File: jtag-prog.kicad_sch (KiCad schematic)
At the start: 38 parts, among them J5 USB_C_Receptacle_USB2.0_14P, J6 Conn_ST_STDC14, U14 AMS1117-3.3, U16 FT2232HQ, U17 93LCxxA, Y2 12Mhz

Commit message: Update the design files
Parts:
- C24: value 10uF -> 1uF
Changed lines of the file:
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@@
 			)
 		)
-		(property "Value" "10uF"
+		(property "Value" "1uF"
 			(at 113.03 67.3162 0)
 			(effects

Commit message: Update the schematic
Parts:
- added D9: D_Schottky, Diode_SMD:D_SOD-123, symbol Device:D_Schottky
- renumbered C18 to C36, C26 to C37, C21 to C38, C22 to C39, C16 to C40, C17 to C41, C48 to C42, C25 to C43, C49 to C44, C24 to C45, C23 to C46, C50 to C47, C54 to C48, C53 to C49, C52 to C50, J5 to J14, J6 to J15, R59 to R56, R35 to R57, R48 to R58, R60 to R59, R62 to R60, R63 to R62, R65 to R63, R66 to R65, R69 to R66, R70 to R67, R67 to R69, U17 to U12, U14 to U13, U16 to U14
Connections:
- net VBUS: now also D9.1 (K); no longer J14.A4 (VBUS), J14.A9 (VBUS), J14.B4 (VBUS), J14.B9 (VBUS)
- new net: D9.2 (A), J14.A4 (VBUS), J14.A9 (VBUS), J14.B4 (VBUS), J14.B9 (VBUS)
- no-connect marks 30 -> 31
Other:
- moved on the sheet: C37, C40, C41, R64, R65, R66, R67, R68, Y2

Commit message: update the  source code
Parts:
- added J20: Conn_01x10, Connector_PinHeader_2.54mm:PinHeader_1x10_P2.54mm_Vertical, symbol Connector_Generic:Conn_01x10
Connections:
- net GND: now also J20.5 (Pin_5)
- net TCK: now also J20.1 (Pin_1)
- net TDI: now also J20.2 (Pin_2)
- net TDO: now also J20.3 (Pin_3)
- net TMS: now also J20.4 (Pin_4)
- net UART_RX: now also J20.6 (Pin_6)
- net UART_TX: now also J20.7 (Pin_7)
- net at U14.40 (BDBUS2): now also J20.8 (Pin_8)
- net at U14.41 (BDBUS3): now also J20.9 (Pin_9)
- net at U14.43 (BDBUS4): now also J20.10 (Pin_10)
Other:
- moved on the sheet: J15

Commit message: Update the source files
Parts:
- removed C37, C42, C47, C48, C49, C50, C51: 100n, Capacitor_SMD:C_0402_1005Metric, symbol Device:C_Small
- removed C40, C41: 10pF, Capacitor_SMD:C_0402_1005Metric, symbol Device:C_Small
- removed C43: 4.7u, Capacitor_SMD:C_0603_1608Metric, symbol Device:C_Small
- removed D9: D_Schottky, Diode_SMD:D_SOD-123, symbol Device:D_Schottky
- removed FB1, FB2: 600R@100Mhz, Inductor_SMD:L_0603_1608Metric, symbol Device:FerriteBead_Small
- removed J14: USB_C_Receptacle_USB2.0_14P, Connector_USB:USB_C_Receptacle_G-Switch_GT-USB-7010ASV, symbol Connector:USB_C_Receptacle_USB2.0_14P
- removed J15: Conn_ST_STDC14, Connector_PinHeader_1.27mm:PinHeader_2x07_P1.27mm_Vertical, symbol Connector:Conn_ST_STDC14
- removed J20: Conn_01x10, Connector_PinHeader_2.54mm:PinHeader_1x10_P2.54mm_Vertical, symbol Connector_Generic:Conn_01x10
- removed R56, R57, R58: 10k, Resistor_SMD:R_0402_1005Metric, symbol Device:R_Small
- removed R59, R60, R69: 2.2k, Resistor_SMD:R_0402_1005Metric, symbol Device:R_Small
- removed R61: 12k@1%, Resistor_SMD:R_0402_1005Metric, symbol Device:R_Small
- removed R62, R63, R64, R65: 0R, Resistor_SMD:R_0402_1005Metric, symbol Device:R_Small
- removed R66, R67, R68: 5.1k, Resistor_SMD:R_0402_1005Metric, symbol Device:R_Small
- removed U12: 93LCxxA, Package_SO:SOIC-8_3.9x4.9mm_P1.27mm, symbol Memory_EEPROM:93LCxxA
- removed U14: FT2232HQ, Package_DFN_QFN:QFN-64-1EP_9x9mm_P0.5mm_EP4.35x4.35mm, symbol Interface_USB:FT2232HQ
- removed Y2: 12Mhz, Crystal:Crystal_SMD_3225-4Pin_3.2x2.5mm, symbol Device:Crystal_GND24_Small
- added C10, C7: 4.7u, Capacitor_SMD:C_0603_1608Metric, symbol Device:C_Small
- added C2, C8, C9: 100n, Capacitor_SMD:C_0402_1005Metric, symbol Device:C_Small
- added C5, C6: 10pF, Capacitor_SMD:C_0402_1005Metric, symbol Device:C_Small
- added D11, D4: RED, LED_SMD:LED_0603_1608Metric, symbol Device:LED_Small
- added J1: USB_C_Receptacle_USB2.0_14P, Connector_USB:USB_C_Receptacle_G-Switch_GT-USB-7010ASV, symbol Connector:USB_C_Receptacle_USB2.0_14P
- added R1, R2: 27R, Resistor_SMD:R_0402_1005Metric, symbol Device:R_Small
- added R12, R3: 10k, Resistor_SMD:R_0402_1005Metric, symbol Device:R_Small
- added R4: 1k, Resistor_SMD:R_0402_1005Metric, symbol Device:R_Small
- added R5, R6: 1.2K, Resistor_SMD:R_0402_1005Metric, symbol Device:R_Small
- added SW1, SW5: BOOT, EasyEDA_Lib:SW-SMD_L3.9-W3.0-P4.45, symbol Switch:SW_Push
- added U10: RP2040, Package_DFN_QFN:QFN-56-1EP_7x7mm_P0.4mm_EP3.2x3.2mm, symbol MCU_RaspberryPi:RP2040
- added U2: W25Q128JVS, Package_SO:SOIC-8_5.3x5.3mm_P1.27mm, symbol Memory_Flash:W25Q128JVS
- added Y1: 12Mhz, Crystal:Crystal_SMD_3225-4Pin_3.2x2.5mm, symbol Device:Crystal_GND24_Small
- C44: value 4.7u -> 100n; footprint Capacitor_SMD:C_0603_1608Metric -> Capacitor_SMD:C_0402_1005Metric
- C45: value 1uF -> 100n; footprint Capacitor_SMD:C_0603_1608Metric -> Capacitor_SMD:C_0402_1005Metric
- renumbered C36 to C1, C38 to C3, C39 to C4, U13 to U1
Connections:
- net +3.3V is gone; now on net +3.3V_JTAG: C3.1, C4.1, U1.2 (VO)
- net VCORE is gone; now on net +3.3V_JTAG: C45.1
- net D+: now also J1.A6 (D+), J1.B6 (D+), R2.1
- net D-: now also J1.A7 (D-), J1.B7 (D-), R1.1
- net GND: now also C44.2, C10.2, C2.1, C5.2, C6.2, C7.2, C8.2, C9.2, D11.1 (K), D4.1 (K), J1.A1 (GND), J1.A12 (GND), J1.B1 (GND), J1.B12 (GND), J1.S1 (SHIELD), SW1.2, SW5.1, U10.57 (GND), U2.4 (GND), Y1.2, Y1.4; no longer C44.1
- net TCK: now also U10.29 (GPIO18)
- net TDI: now also U10.27 (GPIO16)
- net TDO: now also U10.28 (GPIO17)
- net TMS: now also U10.30 (GPIO19)
- net VBUS: now also J1.A4 (VBUS), J1.A9 (VBUS), J1.B4 (VBUS), J1.B9 (VBUS)
- net +3.3V_JTAG: now reaches C46.1
- net +3.3V_JTAG: now also C44.1, C2.2, C7.1, C8.1, R12.2, R3.1, R6.1, U10.1 (IOVDD), U10.10 (IOVDD), U10.22 (IOVDD), U10.33 (IOVDD), U10.42 (IOVDD), U10.43 (ADC_AVDD), U10.44 (VREG_IN), U10.48 (USB_VDD), U10.49 (IOVDD), U2.8 (VCC)
- new net: D11.2 (A), R6.2
- new net: R12.1, SW5.2, U10.26 (RUN)
- new net: D4.2 (A), R5.2
- new net: C6.1, R4.1, Y1.3
- new net +1V: C10.1, C9.1, U10.23 (DVDD), U10.45 (VREG_VOUT), U10.50 (DVDD)
- new net DBG_RX: U10.16 (GPIO13)
- new net DBG_TX: U10.15 (GPIO12)
- new net LED1: R5.1, U10.37 (GPIO25)
- new net QSPI_SCLK: U10.52 (QSPI_SCLK), U2.6 (CLK)
- new net QSPI_SD0: U10.53 (QSPI_SD0), U2.5 (DI/IO_{0})
- new net QSPI_SD1: U10.55 (QSPI_SD1), U2.2 (DO/IO_{1})
- new net QSPI_SD2: U10.54 (QSPI_SD2), U2.3 (~{WP}/IO_{2})
- new net QSPI_SD3: U10.51 (QSPI_SD3), U2.7 (~{HOLD}/~{RESET}/IO_{3})
- new net QSPI_SS: R3.2, SW1.1, U10.56 (QSPI_SS), U2.1 (~{CS})
- new net RST: U10.31 (GPIO20)
- new net SWCLK: U10.24 (SWCLK)
- new net SWD: U10.25 (SWD)
- new net TRST: U10.32 (GPIO21)
- new net USB_N: R1.2, U10.46 (USB_DM)
- new net USB_P: R2.2, U10.47 (USB_DP)
- new net XIN: C5.1, U10.20 (XIN), Y1.1
- new net XOUT: R4.2, U10.21 (XOUT)
- no-connect marks 31 -> 28
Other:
- note added: "Flash Memory"
- note added: "RP2040 MCU"
- moved on the sheet: C1, C3, C4, U1

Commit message: Update the schematic
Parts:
- added U1001: XC6206PxxxMR, Package_TO_SOT_SMD:SOT-23-3, symbol Regulator_Linear:XC6206PxxxMR
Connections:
- net +3.3V_JTAG: now also U1001.2 (VO); no longer U1.2 (VO)
- net GND: now also U1001.1 (GND); no longer U1.1 (GND)
- net VBUS: now also U1001.3 (VI); no longer U1.3 (VI)
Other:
- moved on the sheet: U1
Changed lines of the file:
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@@
 	)
 	(no_connect
+		(at 198.12 134.62)
+	)
+	(no_connect
 		(at 198.12 83.82)
 	)
@@
 	)
 	(no_connect
-		(at 198.12 129.54)
-	)
-	(no_connect
 		(at 147.32 132.08)
 	)
@@
 		)
 	)
-	(label "VDDA"
-		(at 180.34 46.99 0)
-		(effects
-			(font
-				(size 1.27 1.27)
-			)
-			(justify left bottom)
-		)
-	)
 	(label "USB_P"
 		(at 72.39 52.07 180)
@@
 		(on_board yes)
 		(dnp no)
-		(fields_autoplaced yes)
 		(property "Reference" "C1"
 			(at 85.09 34.2962 0)
@@
 	)
 	(symbol
+		(lib_id "Regulator_Linear:XC6206PxxxMR")
+		(at 96.52 31.75 0)
+		(unit 1)
+		(exclude_from_sim no)
+		(in_bom yes)
+		(on_board yes)
+		(dnp no)
+		(property "Reference" "U1001"
+			(at 96.52 25.4 0)
+			(effects
+				(font
+					(size 1.27 1.27)
+				)
+			)
+		)
+		(property "Value" "XC6206PxxxMR"
+			(at 96.52 27.94 0)
+			(effects
+				(font
+					(size 1.27 1.27)
+				)
+			)
+		)
+		(property "Footprint" "Package_TO_SOT_SMD:SOT-23-3"
+			(at 96.52 26.035 0)
+			(effects
+				(font
+					(size 1.27 1.27)
+					(italic yes)
+				)
+				(hide yes)
+			)
+		)
+		(property "Datasheet" "https://www.torexsemi.com/file/xc6206/XC6206.pdf"
+			(at 96.52 31.75 0)
+			(effects
+				(font
+					(size 1.27 1.27)
+				)
+				(hide yes)
+			)
+		)
+		(property "Description" "Positive 60-250mA Low Dropout Regulator, Fixed Output, SOT-23"
+			(at 96.52 31.75 0)
+			(effects
+				(font
+					(size 1.27 1.27)
+				)
+				(hide yes)
+			)
+		)
+		(pin "1"
+		)
+		(pin "3"
+		)
+		(pin "2"
+		)
+		(instances
+			(project "stm32-fpga-bootloader"
+				(path "/5ed49623-6cbc-4a61-8fb3-1814d185ddb6/18a6db22-6310-447a-b64d-8b3f8728a8a2"
+					(reference "U1001")
+					(unit 1)
+				)
+			)
+		)
+	)
+	(symbol
 		(lib_id "power:GND")
 		(at 151.13 43.18 0)
@@
 	(symbol
 		(lib_id "Regulator_Linear:AMS1117-3.3")
-		(at 96.52 31.75 0)
+		(at 53.34 82.55 0)
 		(unit 1)
 		(exclude_from_sim no)
@@
 		(fields_autoplaced yes)
 		(property "Reference" "U1"
-			(at 96.52 25.4 0)
+			(at 53.34 76.2 0)
 			(effects
 				(font
@@
 		)
 		(property "Value" "AMS1117-3.3"
-			(at 96.52 27.94 0)
+			(at 53.34 78.74 0)
 			(effects
 				(font
@@
 		)
 		(property "Footprint" "Package_TO_SOT_SMD:SOT-223-3_TabPin2"
-			(at 96.52 26.67 0)
+			(at 53.34 77.47 0)
 			(effects
 				(font
@@
 		)
 		(property "Datasheet" "http://www.advanced-monolithic.com/pdf/ds1117.pdf"
-			(at 99.06 38.1 0)
+			(at 55.88 88.9 0)
 			(effects
 				(font
@@
 		)
 		(property "Description" "1A Low Dropout regulator, positive, 3.3V fixed output, SOT-223"
-			(at 96.52 31.75 0)
+			(at 53.34 82.55 0)
 			(effects
 				(font

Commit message: Update the schematic
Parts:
- removed U1: AMS1117-3.3, Package_TO_SOT_SMD:SOT-223-3_TabPin2, symbol Regulator_Linear:AMS1117-3.3
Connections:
- net VBUS renamed VBUS3
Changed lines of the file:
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@@
 	)
 	(junction
+		(at 63.5 31.75)
+		(diameter 0)
+		(color 0 0 0 0)
+	)
+	(junction
 		(at 82.55 31.75)
 		(diameter 0)
@@
 	(wire
 		(pts
-			(xy 48.26 31.75) (xy 82.55 31.75)
+			(xy 48.26 31.75) (xy 63.5 31.75)
 		)
 		(stroke
@@
 	(wire
 		(pts
+			(xy 63.5 31.75) (xy 82.55 31.75)
+		)
+		(stroke
+			(width 0)
+			(type default)
+		)
+	)
+	(wire
+		(pts
 			(xy 147.32 96.52) (xy 137.16 96.52)
 		)
@@
 	(wire
 		(pts
+			(xy 63.5 29.21) (xy 63.5 31.75)
+		)
+		(stroke
+			(width 0)
+			(type default)
+		)
+	)
+	(wire
+		(pts
 			(xy 167.64 49.53) (xy 170.18 49.53)
 		)
@@
 	)
 	(symbol
+		(lib_id "power:VBUS")
+		(at 63.5 29.21 0)
+		(unit 1)
+		(exclude_from_sim no)
+		(in_bom yes)
+		(on_board yes)
+		(dnp no)
+		(fields_autoplaced yes)
+		(property "Reference" "#PWR01006"
+			(at 63.5 33.02 0)
+			(effects
+				(font
+					(size 1.27 1.27)
+				)
+				(hide yes)
+			)
+		)
+		(property "Value" "VBUS3"
+			(at 63.5 24.13 0)
+			(effects
+				(font
+					(size 1.27 1.27)
+				)
+			)
+		)
+		(property "Footprint" ""
+			(at 63.5 29.21 0)
+			(effects
+				(font
+					(size 1.27 1.27)
+				)
+				(hide yes)
+			)
+		)
+		(property "Datasheet" ""
+			(at 63.5 29.21 0)
+			(effects
+				(font
+					(size 1.27 1.27)
+				)
+				(hide yes)
+			)
+		)
+		(property "Description" "Power symbol creates a global label with name \"VBUS\""
+			(at 63.5 29.21 0)
+			(effects
+				(font
+					(size 1.27 1.27)
+				)
+				(hide yes)
+			)
+		)
+		(pin "1"
+		)
+		(instances
+			(project "stm32-fpga-bootloader"
+				(path "/5ed49623-6cbc-4a61-8fb3-1814d185ddb6/18a6db22-6310-447a-b64d-8b3f8728a8a2"
+					(reference "#PWR01006")
+					(unit 1)
+				)
+			)
+		)
+	)
+	(symbol
 		(lib_id "power:GND")
 		(at 161.29 43.18 0)
@@
 					(unit 1)
 				)
-			)
-		)
-	)
-	(symbol
-		(lib_id "Regulator_Linear:AMS1117-3.3")
-		(at 53.34 82.55 0)
-		(unit 1)
-		(exclude_from_sim no)
-		(in_bom yes)
-		(on_board yes)
-		(dnp no)
-		(fields_autoplaced yes)
-		(property "Reference" "U1"
-			(at 53.34 76.2 0)
-			(effects
-				(font
-					(size 0.889 0.889)
-				)
-			)
-		)
-		(property "Value" "AMS1117-3.3"
-			(at 53.34 78.74 0)
-			(effects
-				(font
-					(size 0.889 0.889)
-				)
-			)
-		)
-		(property "Footprint" "Package_TO_SOT_SMD:SOT-223-3_TabPin2"
-			(at 53.34 77.47 0)
-			(effects
-				(font
-					(size 1.27 1.27)
-				)
-				(hide yes)
-			)
-		)
-		(property "Datasheet" "http://www.advanced-monolithic.com/pdf/ds1117.pdf"
-			(at 55.88 88.9 0)
-			(effects
-				(font
-					(size 1.27 1.27)
-				)
-				(hide yes)
-			)
-		)
-		(property "Description" "1A Low Dropout regulator, positive, 3.3V fixed output, SOT-223"
-			(at 53.34 82.55 0)
-			(effects
-				(font
-					(size 1.27 1.27)
-				)
-				(hide yes)
-			)
-		)
-		(pin "3"
-		)
-		(pin "2"
-		)
-		(pin "1"
-		)
-		(instances
-			(project "stm32-fpga-bootloader"
-				(path "/5ed49623-6cbc-4a61-8fb3-1814d185ddb6/18a6db22-6310-447a-b64d-8b3f8728a8a2"
-					(reference "U1")
-					(unit 1)
-				)

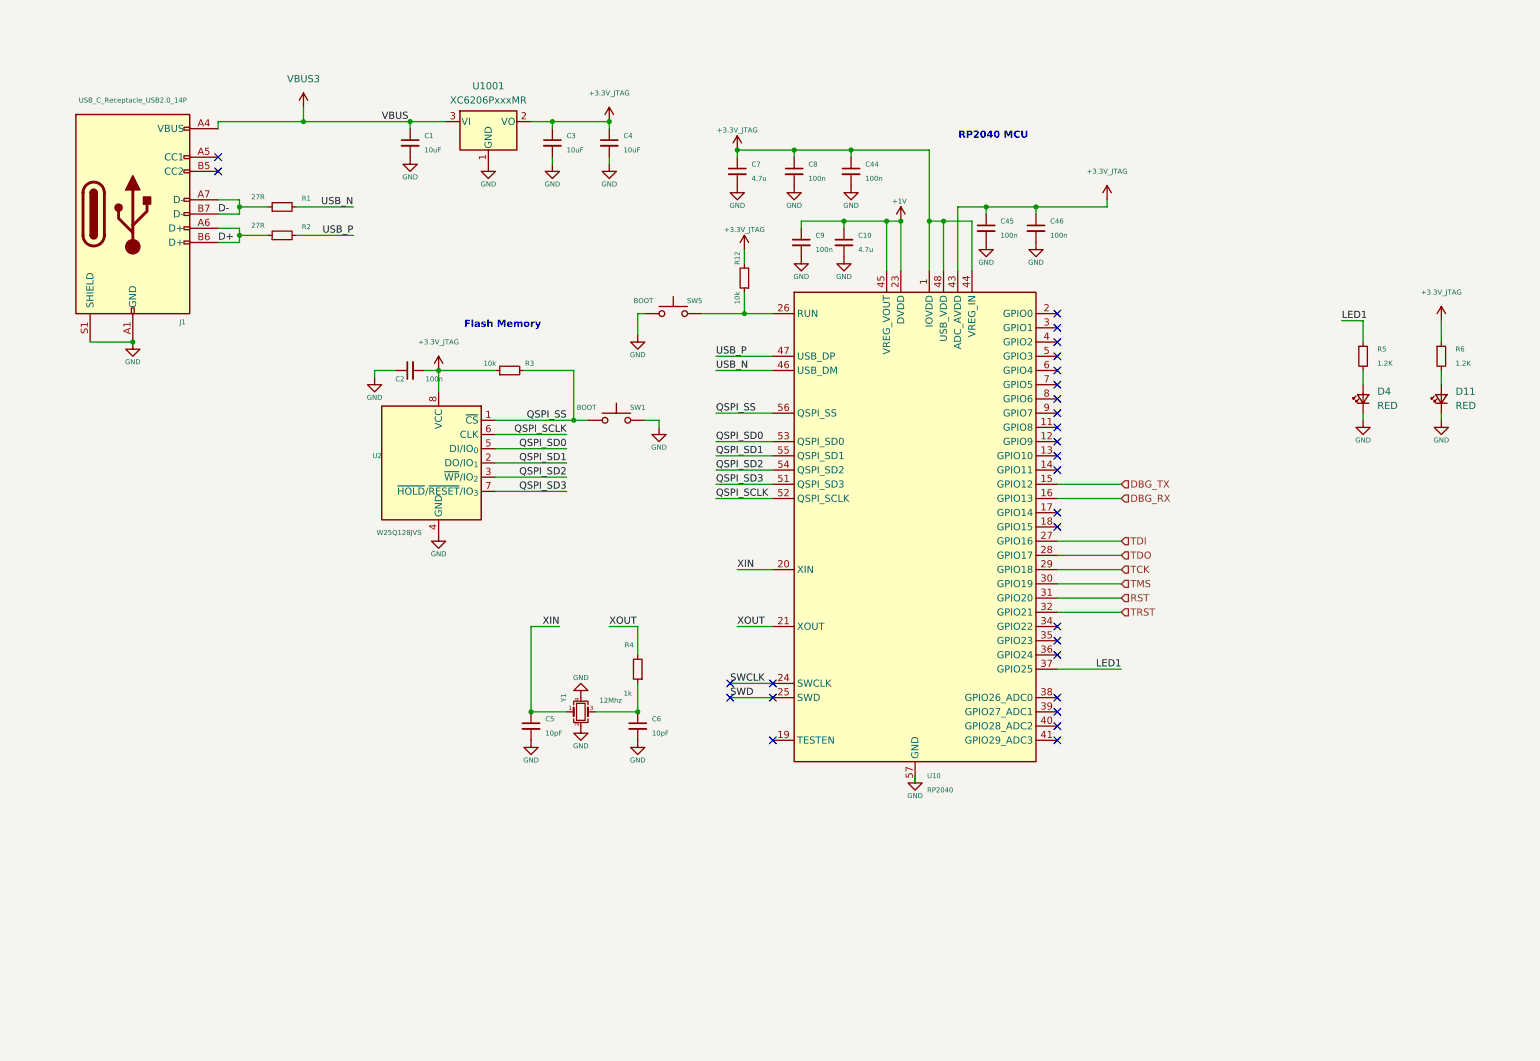
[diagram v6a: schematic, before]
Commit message: Update the footprints
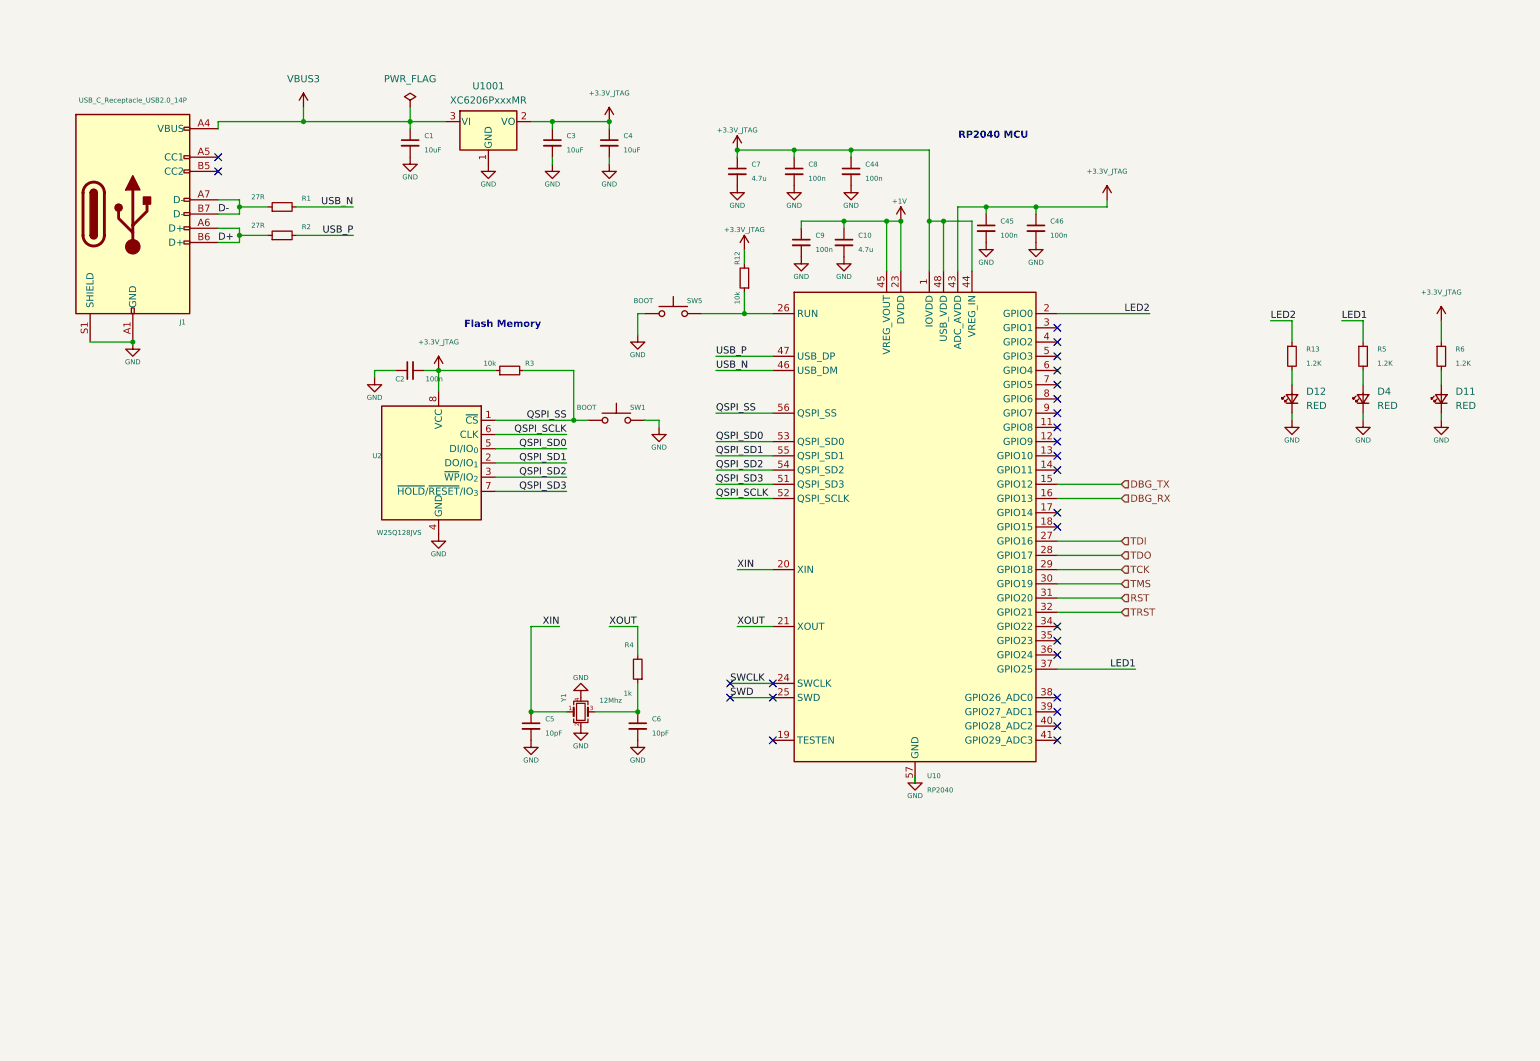
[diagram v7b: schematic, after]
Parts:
- added D12: RED, LED_SMD:LED_0603_1608Metric, symbol Device:LED_Small
- added R13: 1.2K, Resistor_SMD:R_0402_1005Metric, symbol Device:R_Small
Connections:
- net GND: now also D12.1 (K)
- net LED2: now reaches U10.2 (GPIO0)
- net LED2: now also R13.1
- new net: D12.2 (A), R13.2
- no-connect marks 28 -> 27
